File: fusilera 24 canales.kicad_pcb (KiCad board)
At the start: 4 copper layers, 202 parts, among them J1 +12V borne M6, J2 GND borne M5, Q1 MMBT2222A, Q101 MMBT2222A, Q102 MMBT2222A, Q103 MMBT2222A, Q104 MMBT2222A, Q105 MMBT2222A, Q106 MMBT2222A, Q107 MMBT2222A, Q108 MMBT2222A, Q2 MMBT2222A, Q3 MMBT2222A, Q4 MMBT2222A, Q5 MMBT2222A, Q6 MMBT2222A, Q7 MMBT2222A, Q8 MMBT2222A, U1 LM339D, U10 BTS50010-1TAD, U101 LM339D, U102 74HC132D, U103 BTS50010-1TAD, U108 BTS50010-1TAD, U109 74HC132D, U11 BTS50010-1TAD, U110 BTS50010-1TAD, U111 BTS50010-1TAD, U2 74HC132D, U3 BTS50010-1TAD, U4 MCP23017-E/SO, U5 MCP23017-E/SO, U6 LM5164DDA, U7 AP2112K-3.3, U8 BTS50010-1TAD, U9 74HC132D

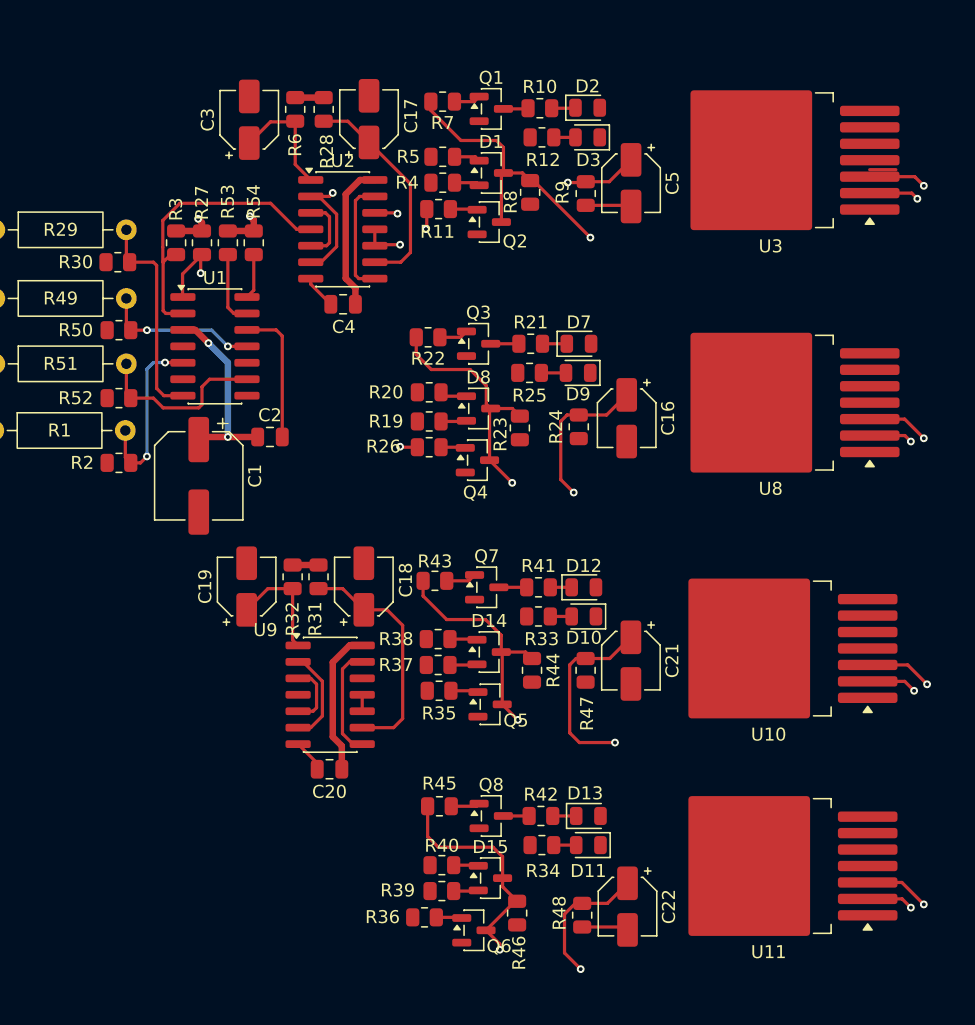
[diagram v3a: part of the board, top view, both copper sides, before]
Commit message: Une GND_PWR con GND y añade el plano de +3,3 V en In2
Sustituye las tres etiquetas GND_PWR del esquemático raíz por símbolos de
tierra para que el bloque de poder comparta la red GND con las celdas. El
plano de In1 pasa a la red GND y se añade el plano de +3,3 V en In2 sobre la
Celda1. Continúa el ruteo de la Celda1 (más vías y pistas en F.Cu e In2) y se
actualiza CONTEXTO_PROYECTO.md.
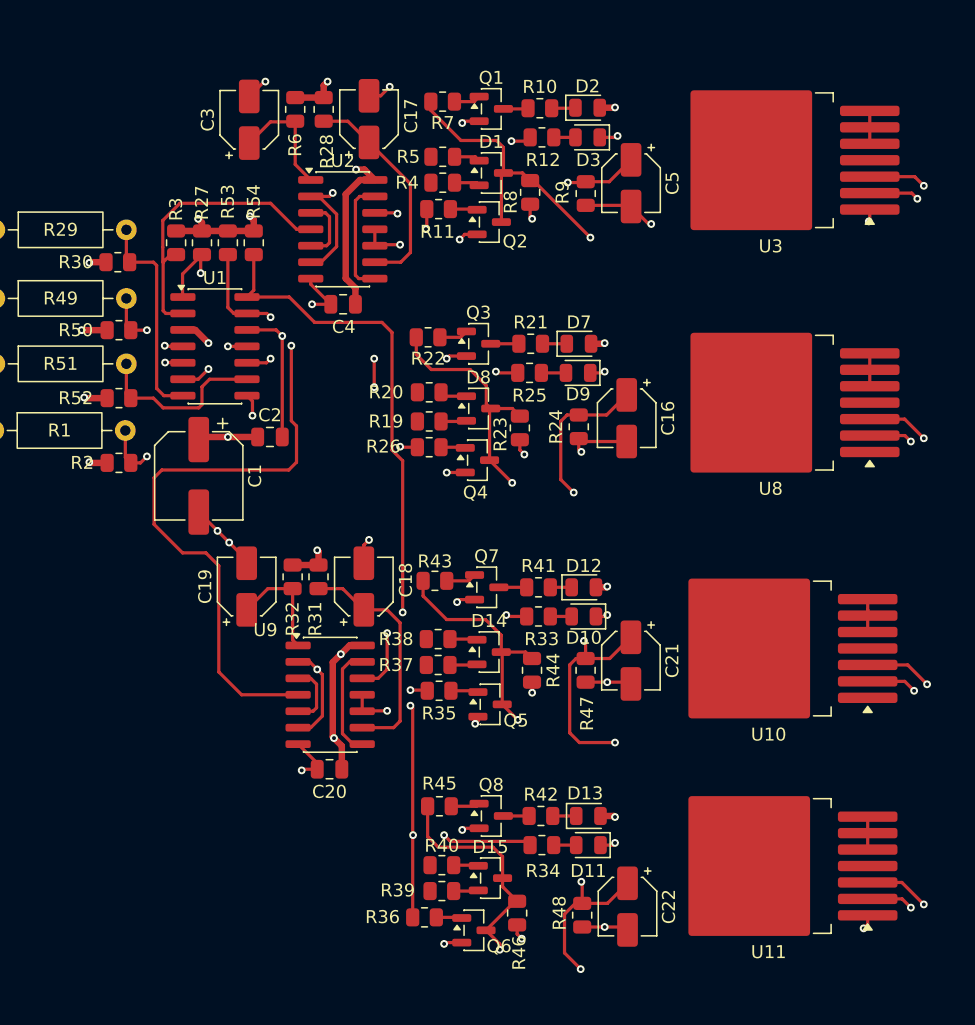
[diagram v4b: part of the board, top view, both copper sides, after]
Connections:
- C11 pad 2: /GND_PWR -> GND
- C14 pad 2: /GND_PWR -> GND
- C15 pad 2: /GND_PWR -> GND
- C7 pad 2: /GND_PWR -> GND
- C8 pad 2: /GND_PWR -> GND
- C9 pad 2: /GND_PWR -> GND
- D5 pad 2: /GND_PWR -> GND
- J2 pad 1: /GND_PWR -> GND
- R14 pad 2: /GND_PWR -> GND
- R15 pad 2: /GND_PWR -> GND
- R18 pad 2: /GND_PWR -> GND
- U6 pad 1: /GND_PWR -> GND
- U6 pad 9: /GND_PWR -> GND
- U7 pad 2: /GND_PWR -> GND
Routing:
- net GND: track 38.8 -> 120.1 mm, vias 0 -> 62
- net Net-(U11-IS): track 45.8 -> 107.0 mm, vias 2 -> 4
- net Net-(R53-Pad1): track 5.75 -> 56.7 mm, vias 0 -> 2
- net Net-(U10-IS): track 47.6 -> 95.8 mm, vias 2 -> 6
- net Net-(R54-Pad1): track 3.49 -> 44.9 mm, vias 0 -> 2
- net Net-(U1A--): track 48.8 -> 89.0 mm, vias 2 -> 3
- net Net-(U1B--): track 47.0 -> 86.4 mm, vias 2 -> 3
- net /GND_PWR: track 34.9 -> 0.00 mm, vias 32 -> 0
- net /Celda1/FALLA4: track 1.27 -> 31.0 mm, vias 0 -> 4
- net /Celda1/FALLA3: track 7.43 -> 30.9 mm, vias 0 -> 3
- net /Celda1/FALLA1: track 20.6 -> 35.4 mm, vias 2 -> 3
- net /Celda1/FALLA2: track 20.2 -> 29.5 mm, vias 2 -> 3
- net +3.3V: track 48.4 -> 57.7 mm, vias 4 -> 17
- net /Celda1/OUT3: track 0.00 -> 2.98 mm
- net /Celda1/OUT2: track 0.00 -> 2.54 mm
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- added copper zone on In2.Cu, net +3.3V
- added copper zone on In1.Cu, net GND
- removed copper zone on In1.Cu, net /GND_PWR

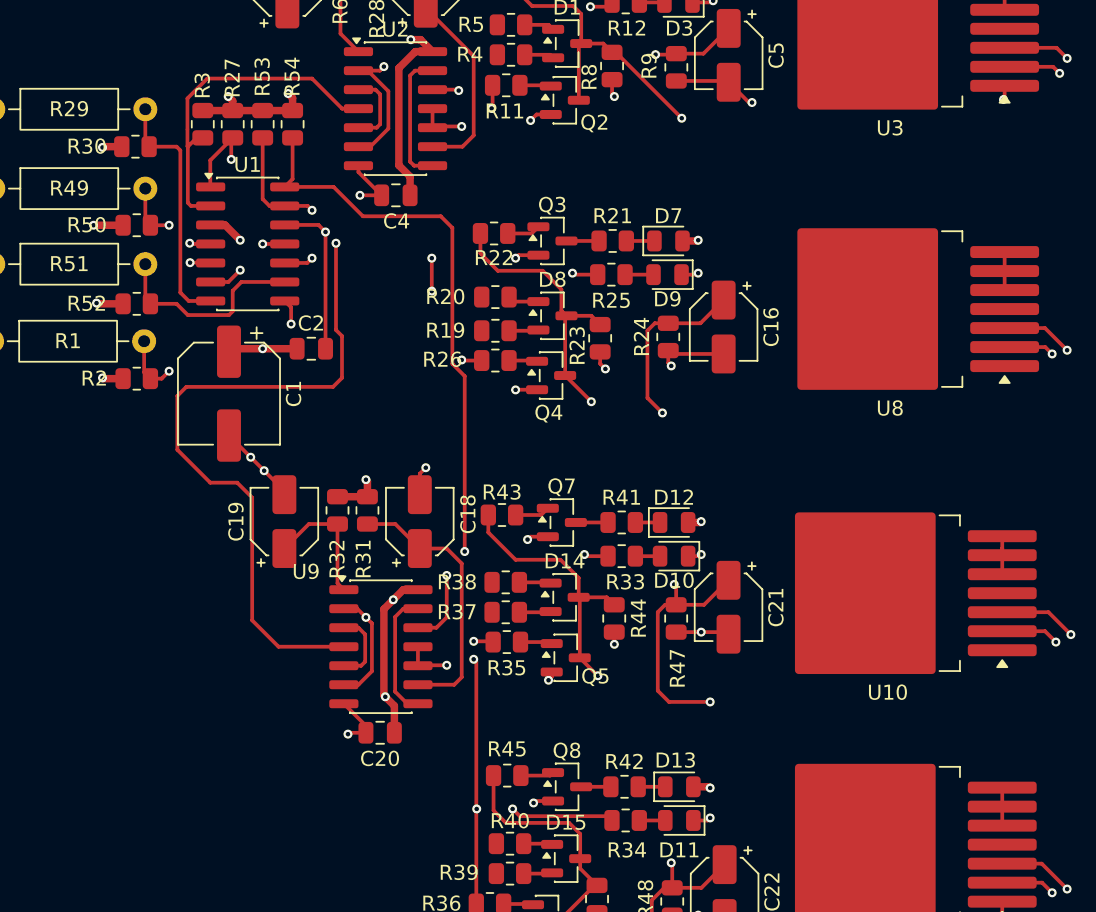
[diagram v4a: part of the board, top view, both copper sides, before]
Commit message: Corrige espaciados de 0,2 mm en la Celda1 y alimenta U1 con un puente en B.Cu
Separa a 0,25 mm o más las pistas de F.Cu y las vías de In2 que quedaban a
0,200 mm (FALLA3, FALLA4, R54, R3, U1B+, IS del canal 1 y vías de GND, R27 y
U1A+), y reordena R27 frente a FALLA1 y U1A- en In2. El pin 3 de U1 estaba en
una isla del plano de +3,3 V encerrada por pistas de In2; se añade un puente de
0,5 mm en B.Cu que la une al plano. Se actualiza CONTEXTO_PROYECTO.md.
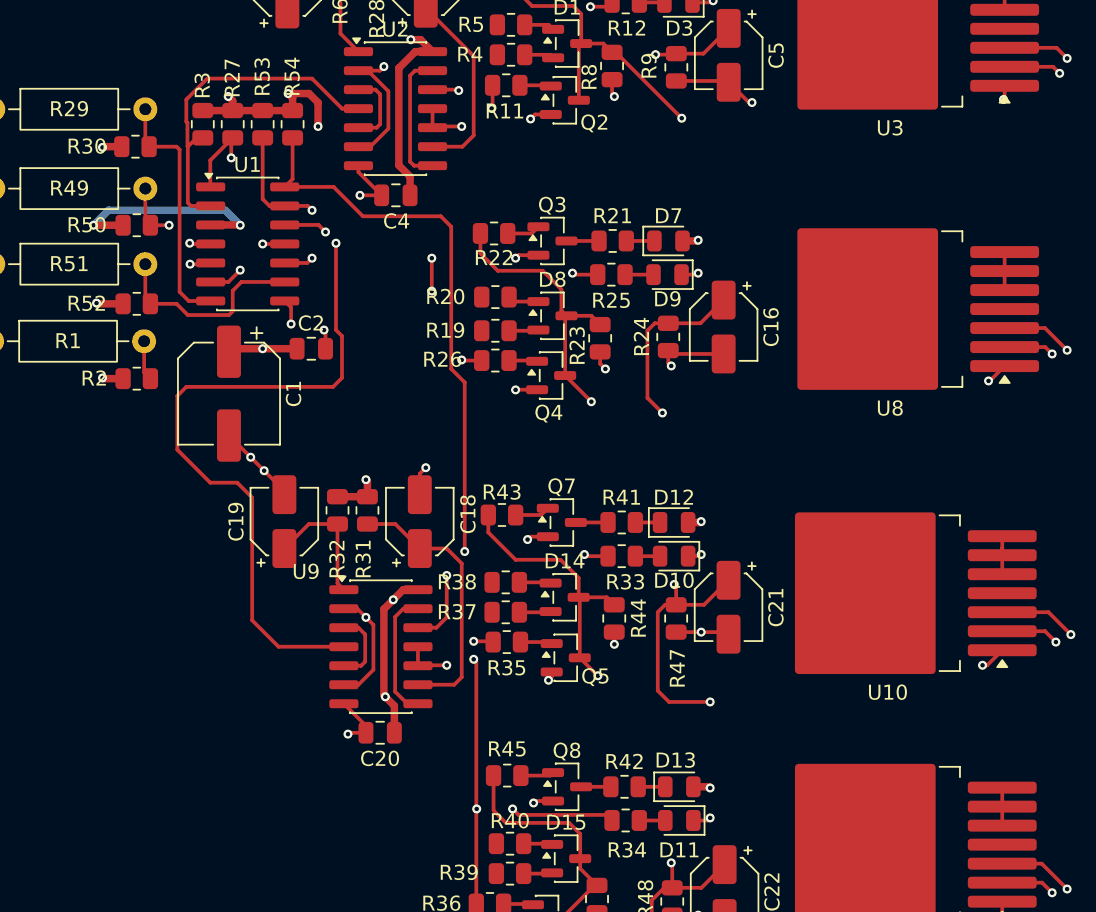
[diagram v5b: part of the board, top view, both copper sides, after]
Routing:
- net +3.3V: track 57.7 -> 71.6 mm, vias 17 -> 18
- net GND: track 120.1 -> 116.8 mm, vias 62 -> 65
- net Net-(U1A-+): track 13.6 -> 12.0 mm, vias 2 -> 1
- net Net-(R27-Pad1): track 27.2 -> 26.2 mm

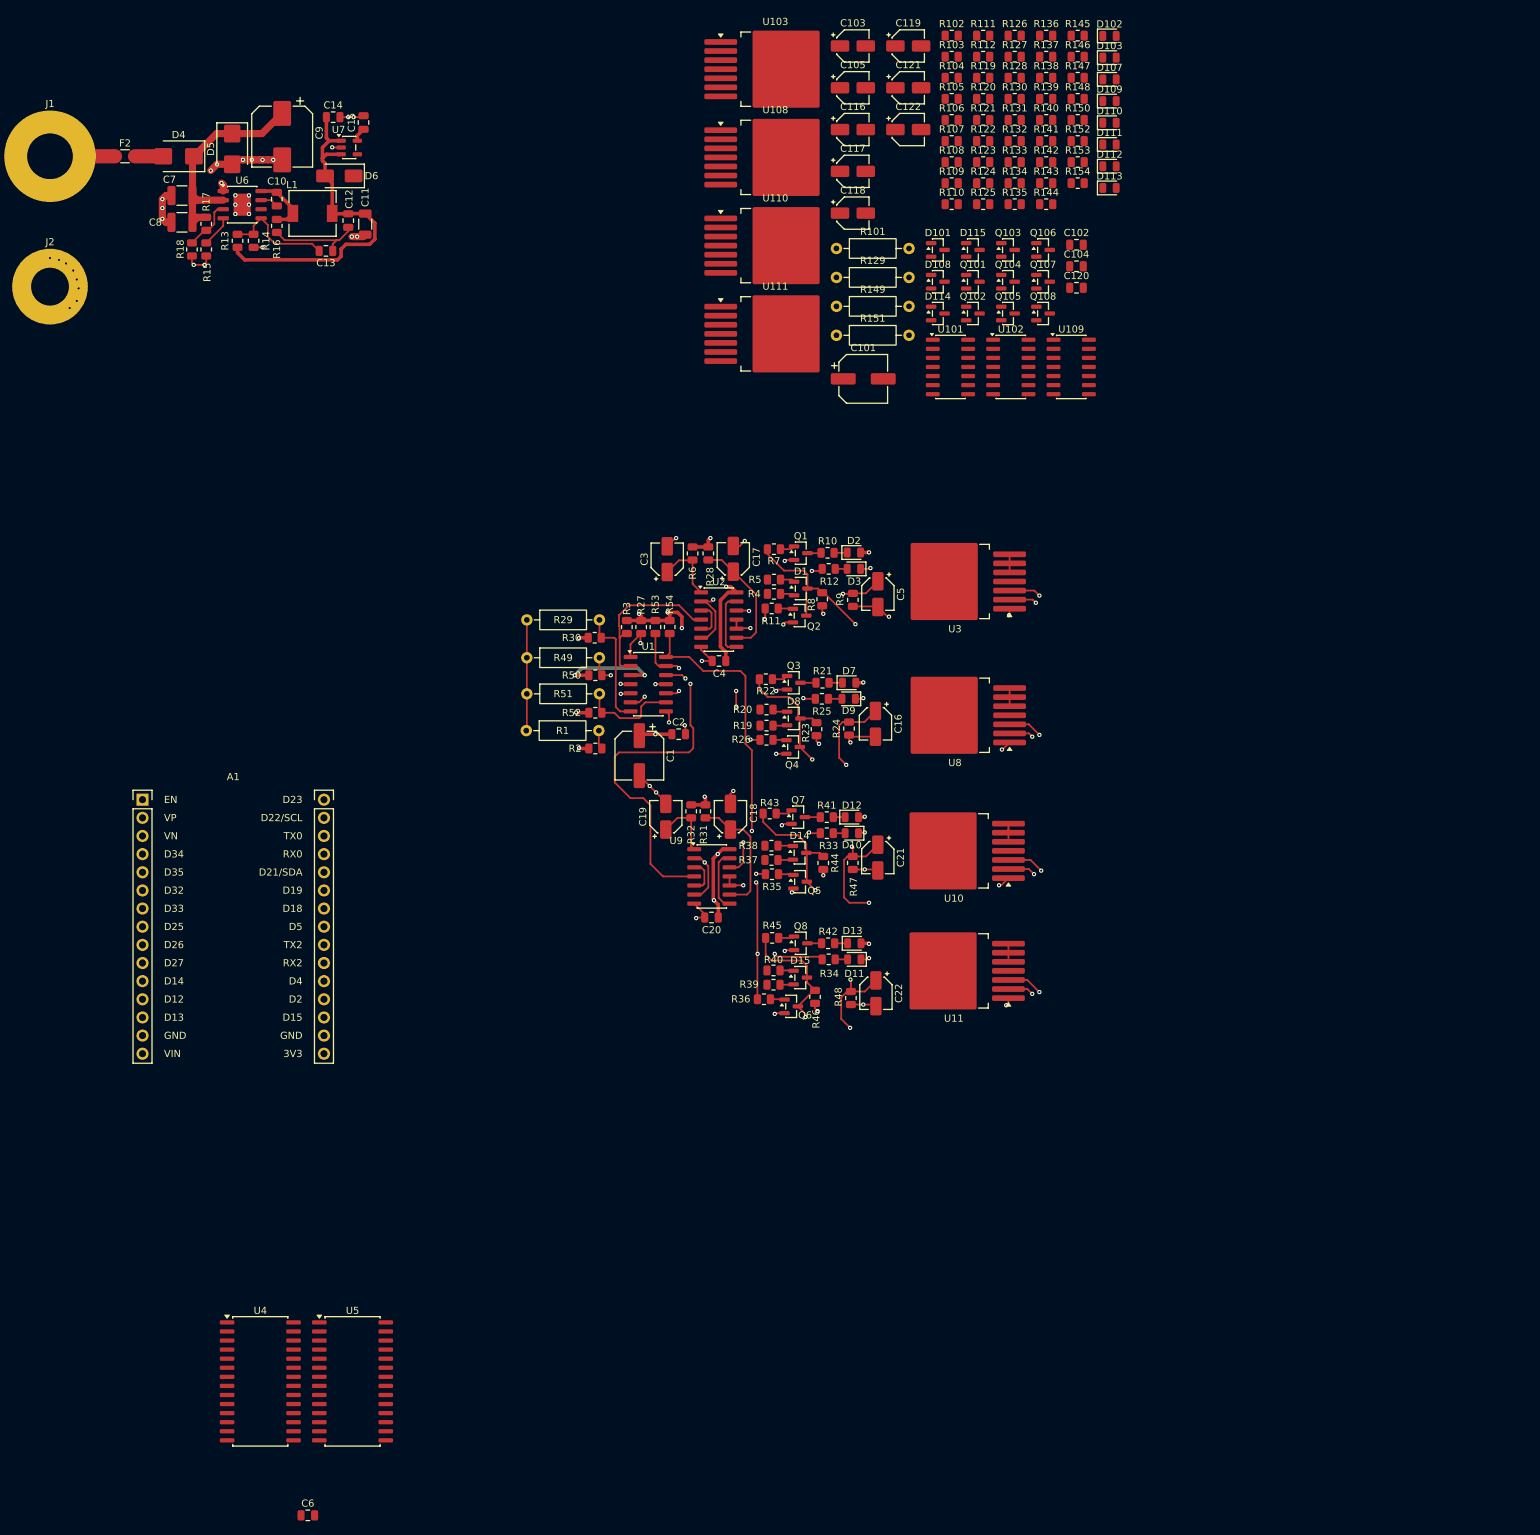
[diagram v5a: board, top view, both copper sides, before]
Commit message: Replica la Celda1 en la Celda2 y extiende los planos de GND y +3,3 V
Copia footprints, pistas y vías de la Celda1 a la Celda2 con la red equivalente
(87 footprints, 539 pistas, 97 vías). Las celdas quedan una junto a la otra, la
Celda2 girada 180°, y los planos de In1 e In2 cubren ahora ambas celdas.
Quedan por resolver la tira de +12 V, las zonas de salida y el contorno. Se
actualiza CONTEXTO_PROYECTO.md.
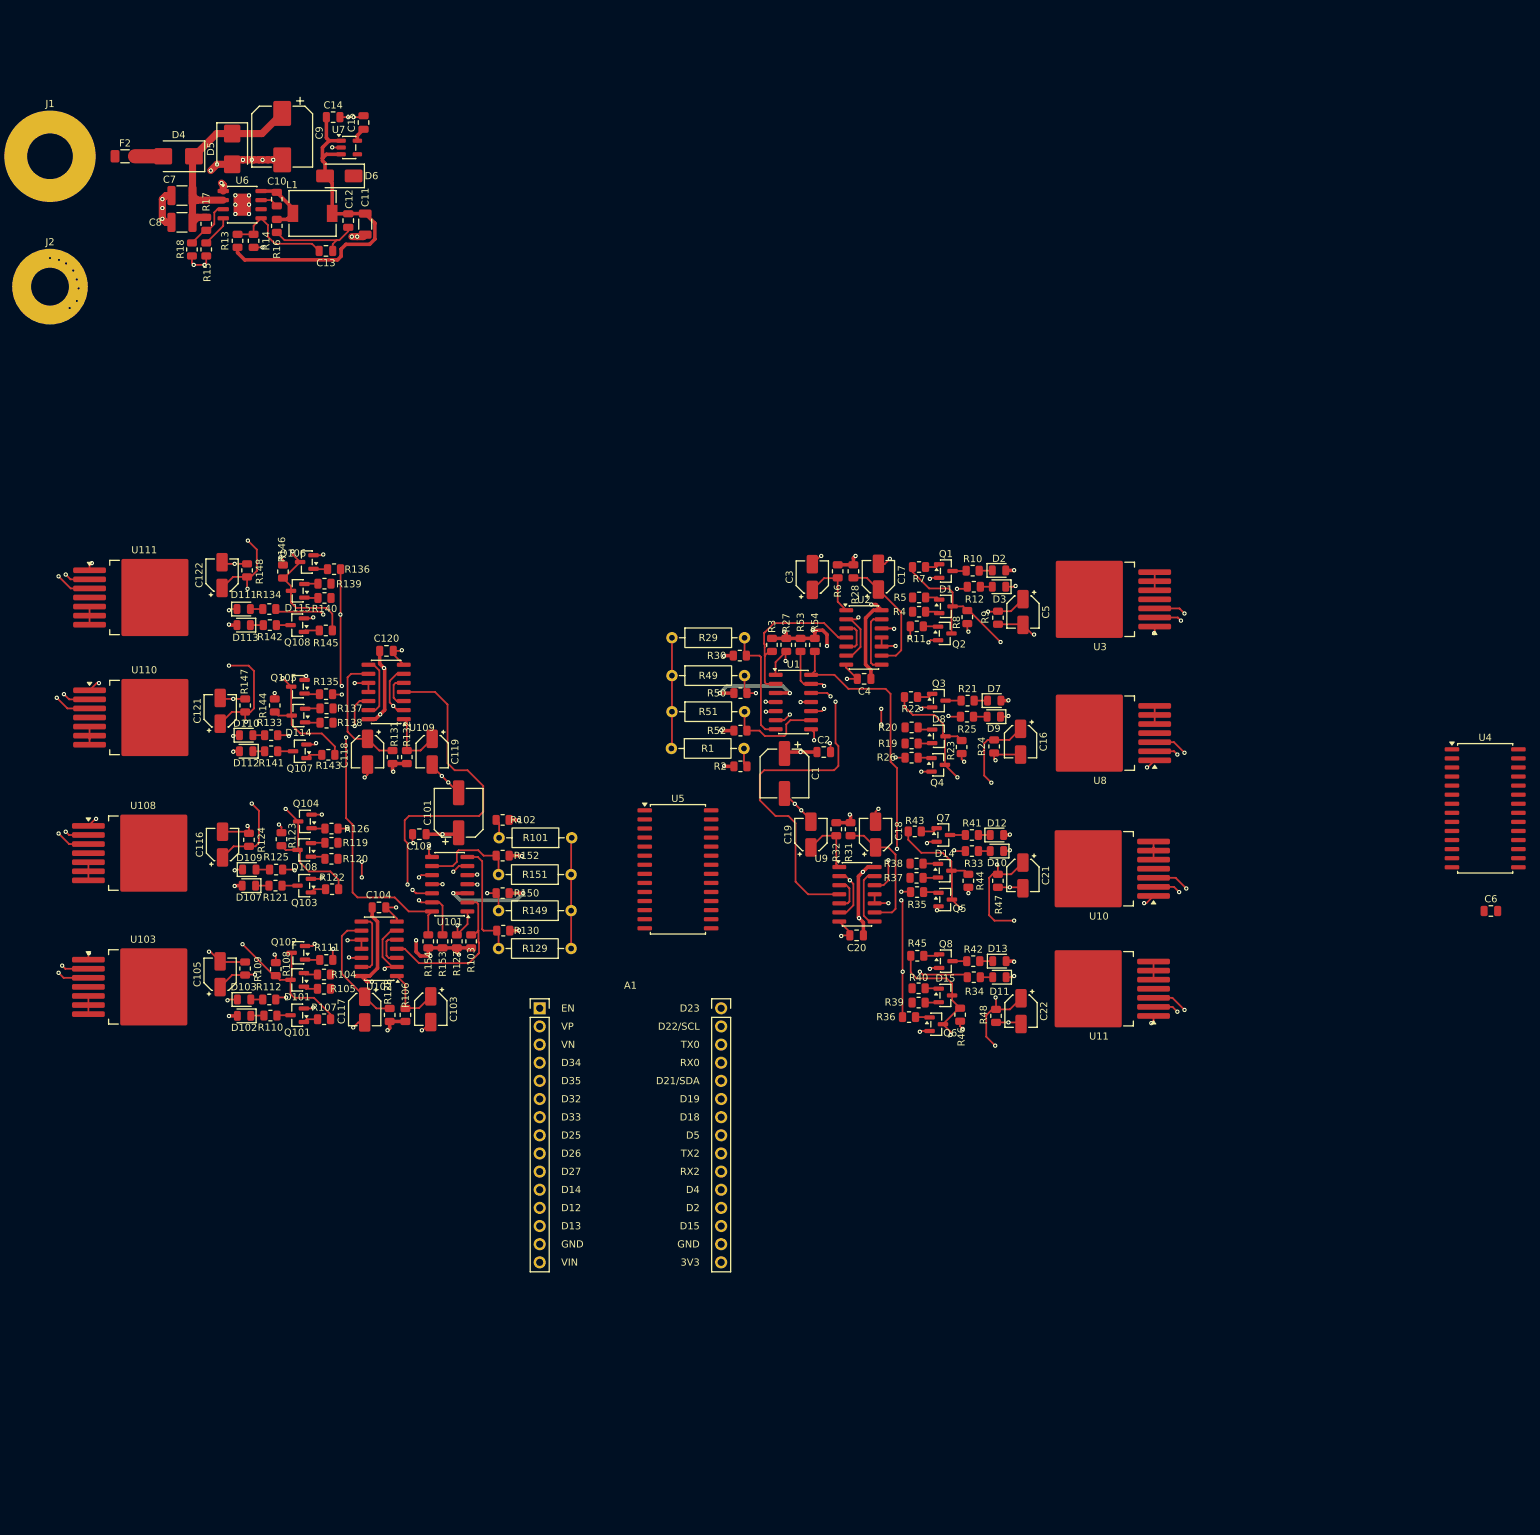
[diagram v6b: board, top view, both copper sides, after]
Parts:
- moved U4 189.3 mm to (222.7, 134.0)
- moved C6 186.0 mm to (223.4, 148.4)
- moved D102 183.0 mm to (48.9, 163.1), turned to 180 degrees
- moved D103 179.0 mm to (48.9, 160.8)
- moved R112 165.5 mm to (52.4, 160.8), turned to 180 degrees
- moved D107 165.1 mm to (49.6, 144.8), turned to 180 degrees
- moved D109 161.5 mm to (49.6, 142.6)
- moved R111 158.7 mm to (60.4, 155.2)
- moved R128 157.7 mm to (69.3, 162.9), turned to -90 degrees
- moved U103 156.0 mm to (34.8, 159.0)
- moved R104 153.2 mm to (60.1, 157.3), turned to 180 degrees
- moved C105 152.5 mm to (45.6, 157.3), turned to 90 degrees
- moved R105 152.4 mm to (60.1, 159.3)
- moved R107 151.1 mm to (60.1, 163.6)
- moved R110 148.3 mm to (52.6, 163.0), turned to 180 degrees
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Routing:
- net Net-(U101D--): track 0.00 -> 107.0 mm, vias 0 -> 4
- net Net-(U101C--): track 0.00 -> 95.8 mm, vias 0 -> 6
- net Net-(U101A--): track 0.00 -> 88.7 mm, vias 0 -> 3
- net Net-(U101B--): track 0.00 -> 86.4 mm, vias 0 -> 3
- net GND: track 116.8 -> 198.6 mm, vias 65 -> 98
- net +3.3V: track 71.6 -> 143.2 mm, vias 18 -> 36
- net Net-(Q106-C): track 0.00 -> 56.8 mm, vias 0 -> 2
- net Net-(R153-Pad1): track 0.00 -> 56.7 mm, vias 0 -> 2
- net Net-(Q105-C): track 0.00 -> 55.8 mm, vias 0 -> 2
- net Net-(Q104-C): track 0.00 -> 55.6 mm, vias 0 -> 2
- net Net-(Q102-C): track 0.00 -> 53.7 mm, vias 0 -> 2
- net Net-(R154-Pad1): track 0.00 -> 44.9 mm, vias 0 -> 2
- net /Celda2/FALLA1: track 0.00 -> 35.4 mm, vias 0 -> 3
- net /Celda2/FALLA3: track 0.00 -> 30.9 mm, vias 0 -> 3
- net /Celda2/FALLA4: track 0.00 -> 30.5 mm, vias 0 -> 4
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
